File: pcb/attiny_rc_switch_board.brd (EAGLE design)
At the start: 11.4 x 17.8 mm, 14 parts, among them U1 ATTINY85-20SU, U2 MOSFET_N-CH_IRLML2502TRPBFPG-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

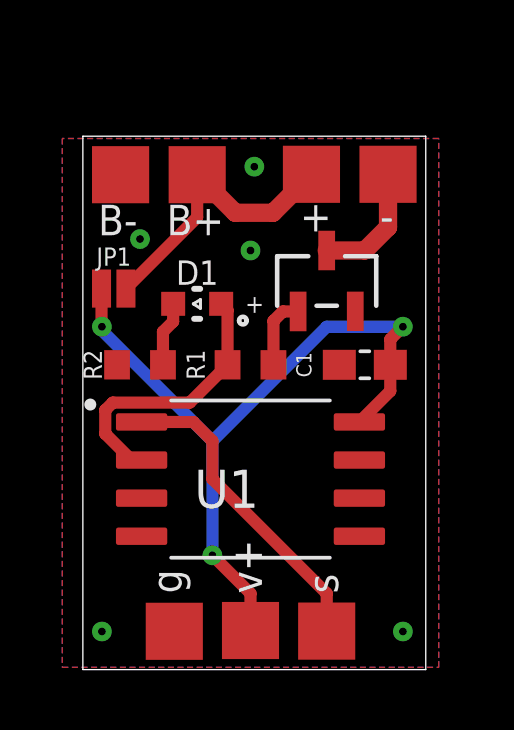
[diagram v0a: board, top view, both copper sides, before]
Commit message: fixed signal pin, changed pads
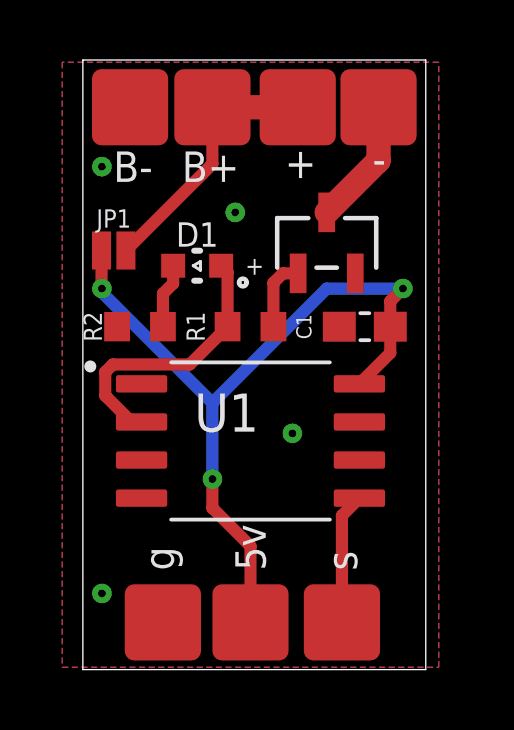
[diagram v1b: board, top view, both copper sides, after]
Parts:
- removed U$8: SMD_PAD, scotts-library:SMD_PAD
- added U$7: SMD_PAD_NO_STENCIL, scotts-library:SMD_PAD_NO_STENCIL
- U$1, U$2, U$3, U$4, U$5, U$6: value SMD_PAD -> SMD_PAD_NO_STENCIL; device scotts-library:SMD_PAD -> scotts-library:SMD_PAD_NO_STENCIL
- moved U$6 8.88 mm to (2.34, 18.7)
- moved U$3 6.45 mm to (10.6, 18.7)
- moved U$4 6.32 mm to (7.92, 18.7)
- moved U$5 3.99 mm to (5.08, 18.7)
- moved U$1 3.06 mm to (9.40, 1.57), turned to 0 degrees
- moved U$2 2.56 mm to (6.35, 1.57), turned to 0 degrees
- moved JP1 1.27 mm to (1.79, 14.0)
- moved U1 1.27 mm to (6.35, 7.62)
- moved C1 1.27 mm to (10.2, 11.4)
- moved D1 1.27 mm to (4.57, 13.5)
- moved R1 1.27 mm to (6.35, 11.4)
- moved R2 1.27 mm to (2.67, 11.4)
- moved U2 1.27 mm to (8.89, 14.2)
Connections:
- removed net PB0: U1.5
- new net PB5: U1.1
- net 5V: now also U$2.P$1; no longer U$1.P$1
- net GND: now also U$6.P$1, U$7.P$1; no longer U$2.P$1, U$4.P$1
- net OUT+: now also U$4.P$1; no longer U$3.P$1
- net OUT-: now also U$3.P$1; no longer U$6.P$1
- net SIG: now also U$1.P$1, U1.5; no longer U$8.P$1, U1.1
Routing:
- net SIG: track 10.5 -> 4.38 mm
- net 5V: track 25.2 -> 26.2 mm
- net OUT+: track 9.65 -> 8.81 mm
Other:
- board size 11.4 x 17.8 mm -> 11.4 x 20.3 mm
- board text added: "5v"
- board text removed: "v+"

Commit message: fixed output pads
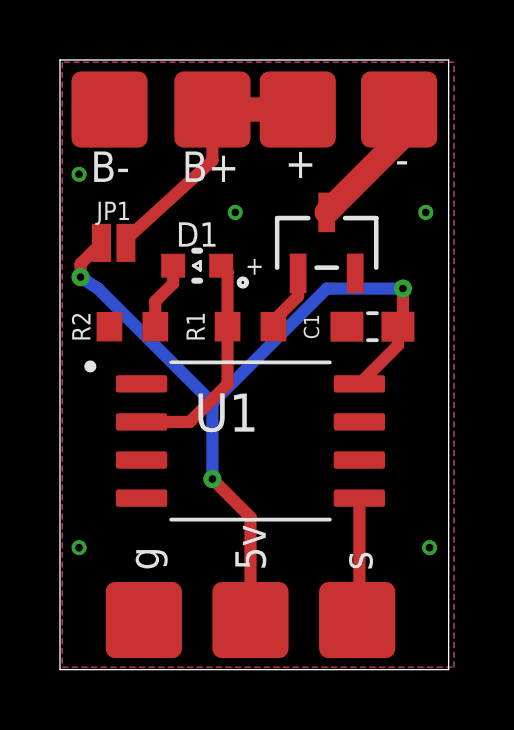
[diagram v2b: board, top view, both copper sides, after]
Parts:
- moved U$3 0.69 mm to (11.3, 18.7)
- moved U$6 0.69 mm to (1.65, 18.7)
- moved U$7 0.64 mm to (2.79, 1.65)
- moved U$1 0.51 mm to (9.91, 1.65)
- moved R2 0.25 mm to (2.41, 11.4)
- moved C1 0.25 mm to (10.4, 11.4)
- moved JP1 0.25 mm to (1.79, 14.2)
- moved U$2 0.08 mm to (6.35, 1.65)
- moved U$4 0.08 mm to (7.92, 18.7)
- moved U$5 0.08 mm to (5.08, 18.7)
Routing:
- net N$1: track 9.18 -> 7.42 mm
- net 5V: track 26.2 -> 27.1 mm
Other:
- board size 11.4 x 20.3 mm -> 13 x 20.3 mm
